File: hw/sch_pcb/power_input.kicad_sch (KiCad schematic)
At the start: 22 parts, among them J2 WAGO 256 ORANGE, J3 WAGO 256 BLUE, J4 HEADER_2x01_PARALLEL, U3 SPV1040

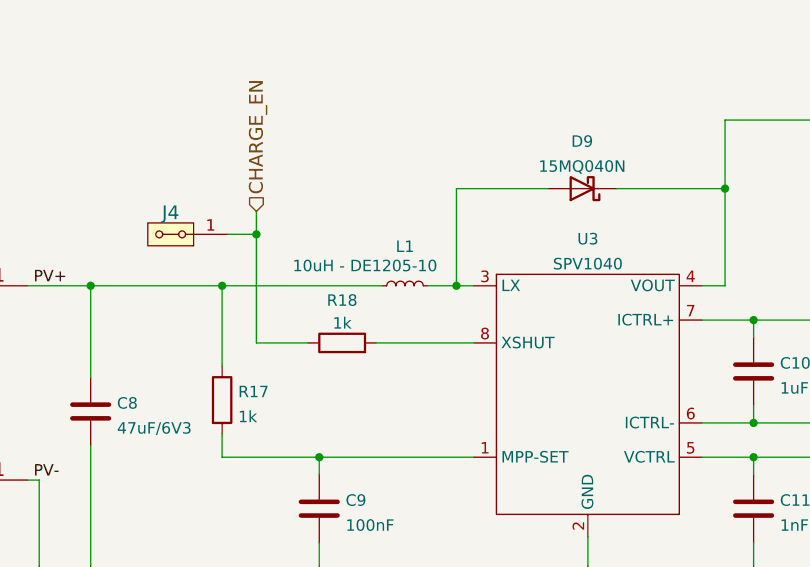
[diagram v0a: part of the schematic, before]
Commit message: Add datasheet to the used LTO cells. Improve documentation, update KiCAD project.
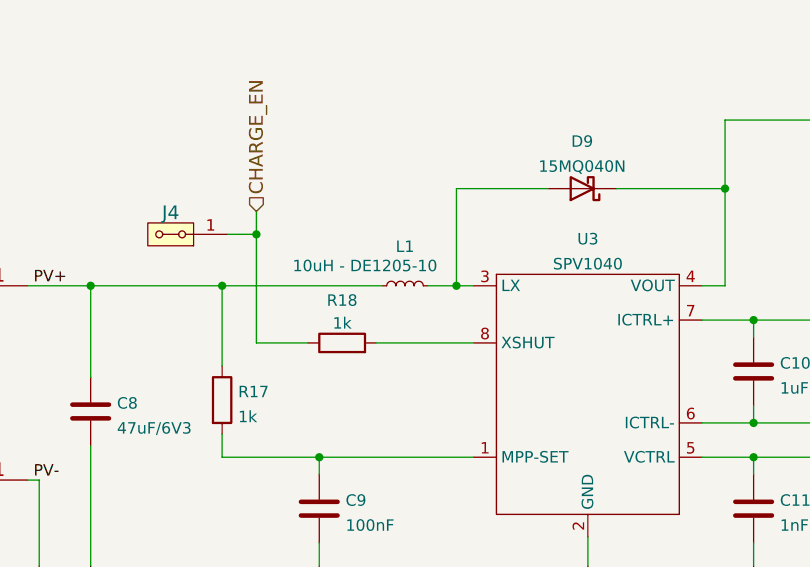
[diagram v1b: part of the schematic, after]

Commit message: Improved documentation and schematics. Output divider values changed to better fit maximum cell voltage.
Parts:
- D10: now not fitted
- R22: value 110k -> 115k; UST_ID 5e3ffc4a1287502a33bad850 -> (none)
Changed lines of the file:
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@@
 		(in_bom yes)
 		(on_board yes)
-		(dnp no)
+		(dnp yes)
 		(fields_autoplaced yes)
 		(property "Reference" "D10"
@@
 		(fields_autoplaced yes)
 		(property "Reference" "R22"
-			(at 224.663 92.4365 0)
+			(at 224.663 92.1328 0)
 			(effects
 				(font
@@
 			)
 		)
-		(property "Value" "110k"
-			(at 224.663 95.2116 0)
+		(property "Value" "115k"
+			(at 224.663 94.5571 0)
 			(effects
 				(font
@@
 			)
 		)
-		(property "UST_ID" "5e3ffc4a1287502a33bad850"
+		(property "UST_ID" ""
 			(at 222.885 93.345 0)
 			(effects
